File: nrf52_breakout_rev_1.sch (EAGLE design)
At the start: 23 parts, among them IC1 E73_2G4M04S

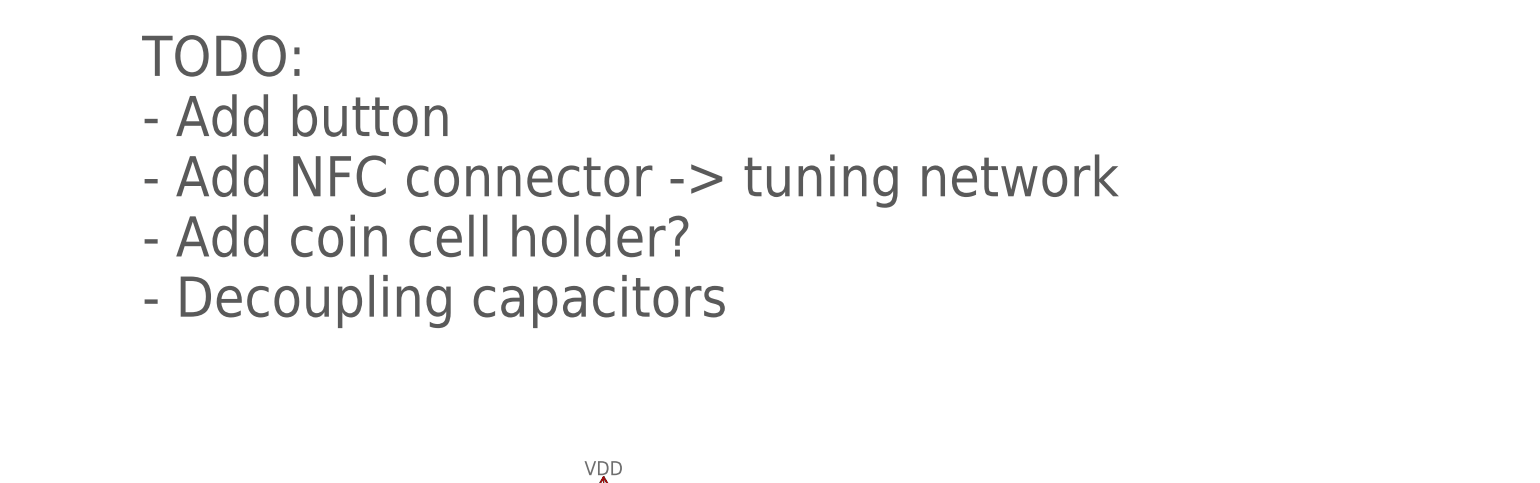
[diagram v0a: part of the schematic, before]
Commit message: added some stuff to the silkscreen
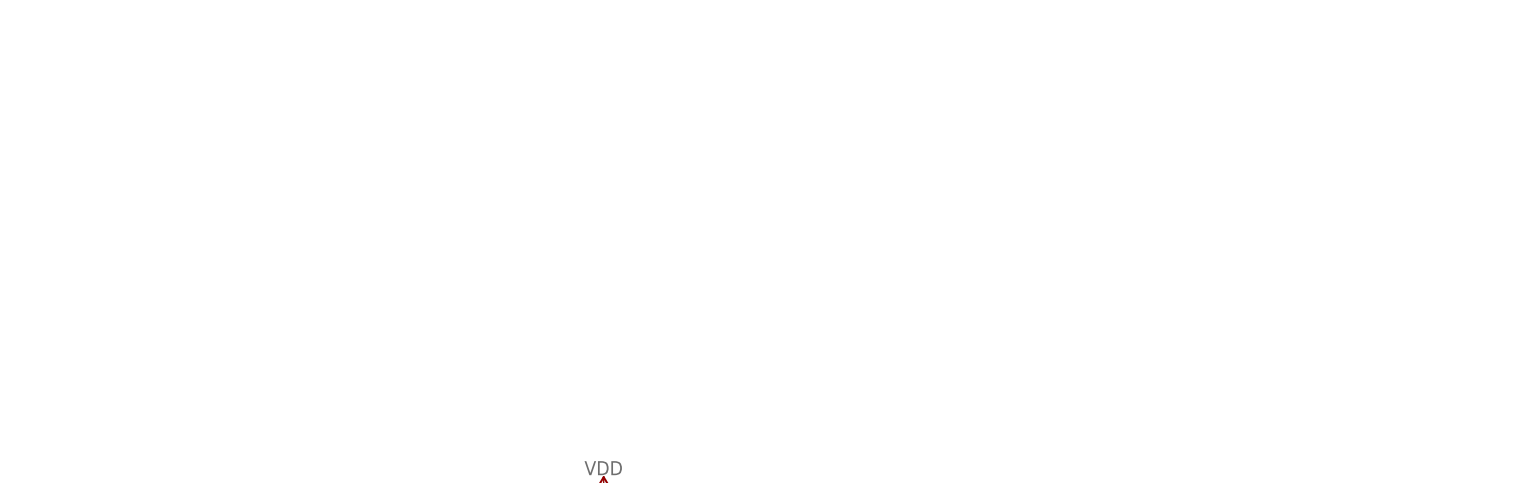
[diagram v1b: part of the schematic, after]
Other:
- note removed: "TODO: - Add button - Add NFC connector -> tuning network - Add coin cell holder? - Decoupling capacitors"
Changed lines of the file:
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@@
 <sheet>
 <plain>
-<text x="83.82" y="195.58" size="5.08" layer="97">TODO:
-- Add button
-- Add NFC connector -&gt; tuning network
-- Add coin cell holder?
-- Decoupling capacitors</text>
 <text x="118.364" y="50.292" size="2.032" layer="97">i2c address: 0x1C</text>
 </plain>
@@
 </drawing>
 <compatibility>
-<note version="6.3" minversion="6.2.2" severity="warning">
-Since Version 6.2.2 text objects can contain more than one line,
-which will not be processed correctly with this version.
-</note>
 <note version="8.2" severity="warning">
 Since Version 8.2, EAGLE supports online libraries. The ids

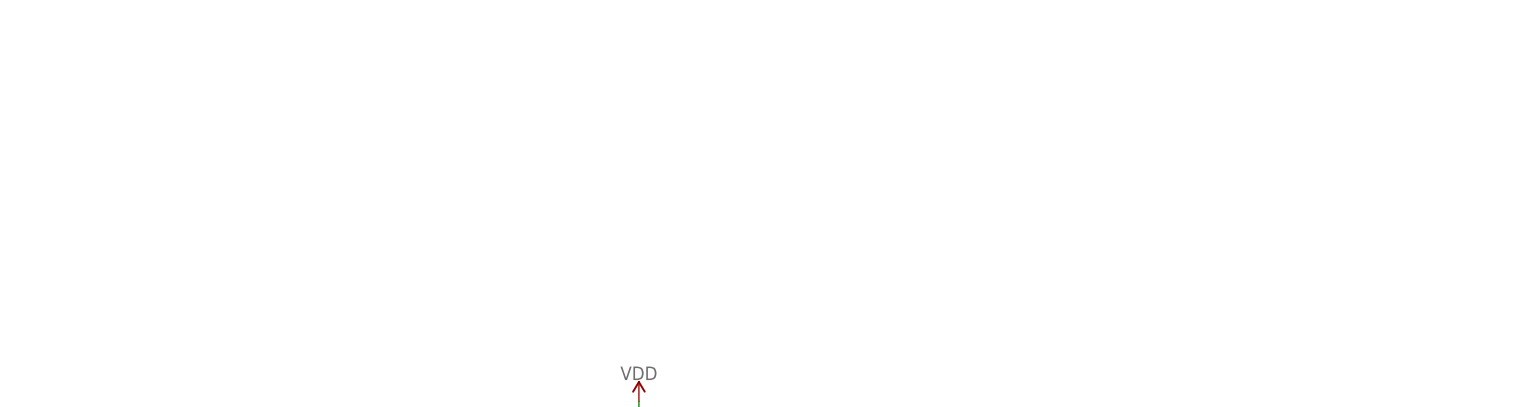
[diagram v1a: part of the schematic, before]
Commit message: added todo list
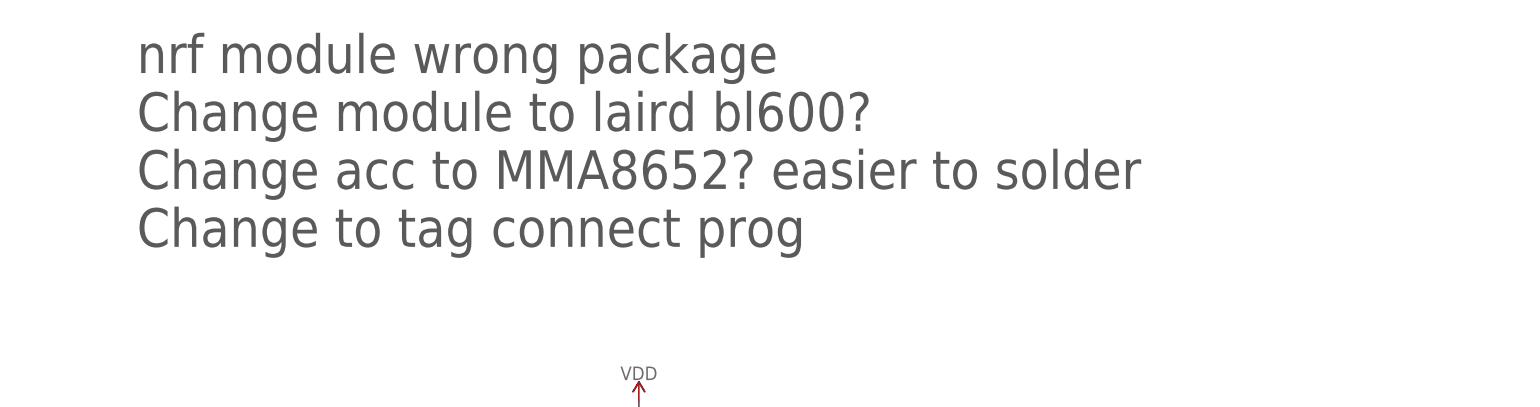
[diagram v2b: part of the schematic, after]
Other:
- note added: "nrf module wrong package Change module to laird bl600? Change acc to MMA8652? easier to solder Change to tag connect prog"
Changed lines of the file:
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@@
 <?xml version="1.0" encoding="utf-8"?>
 <!DOCTYPE eagle SYSTEM "eagle.dtd">
-<eagle version="8.6.3">
+<eagle version="9.1.3">
 <drawing>
 <settings>
@@
 <plain>
 <text x="118.364" y="50.292" size="2.032" layer="97">i2c address: 0x1C</text>
+<text x="76.2" y="193.04" size="5.08" layer="97">nrf module wrong package
+Change module to laird bl600?
+Change acc to MMA8652? easier to solder
+Change to tag connect prog</text>
 </plain>
 <instances>
@@
 </drawing>
 <compatibility>
+<note version="6.3" minversion="6.2.2" severity="warning">
+Since Version 6.2.2 text objects can contain more than one line,
+which will not be processed correctly with this version.
+</note>
 <note version="8.2" severity="warning">
 Since Version 8.2, EAGLE supports online libraries. The ids
